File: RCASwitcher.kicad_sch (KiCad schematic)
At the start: 11 parts, among them J1 Connector_RCA_2x3_REB, J2 Connector_RCA_2x3_REB, J3 Connector_RCA_2x3_REB, J4 Connector_RCA_2x3_REB, J5 Connector_RCA_2x3_REB, J6 Connector_RCA_2x3_REB, SW1 SW_SPDT_3x2_REB, SW2 SW_SPDT_3x2_REB, SW3 SW_SPDT_3x2_REB, SW4 SW_SPDT_3x2_REB, SW5 SW_SPDT_3x2_REB

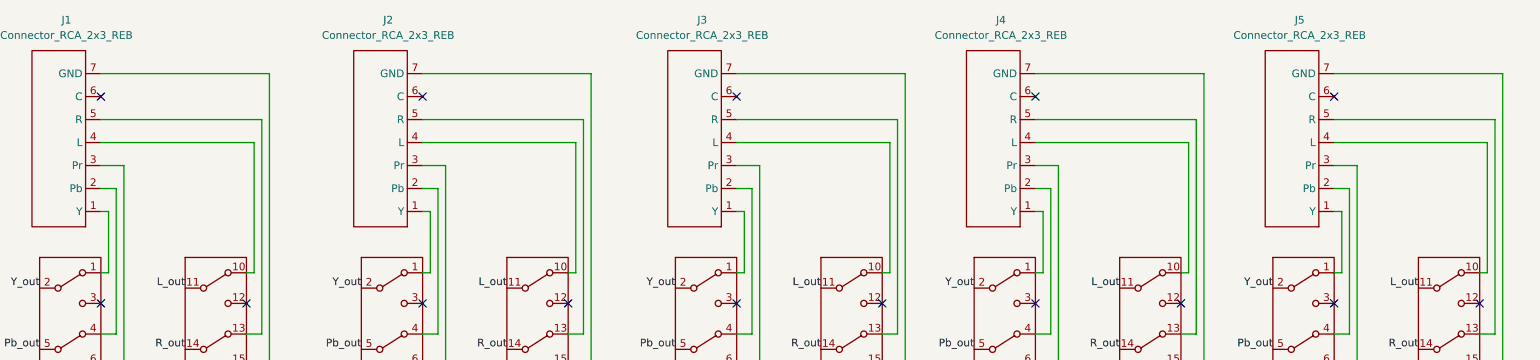
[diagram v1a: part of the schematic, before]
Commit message: Name remaining nets for checking
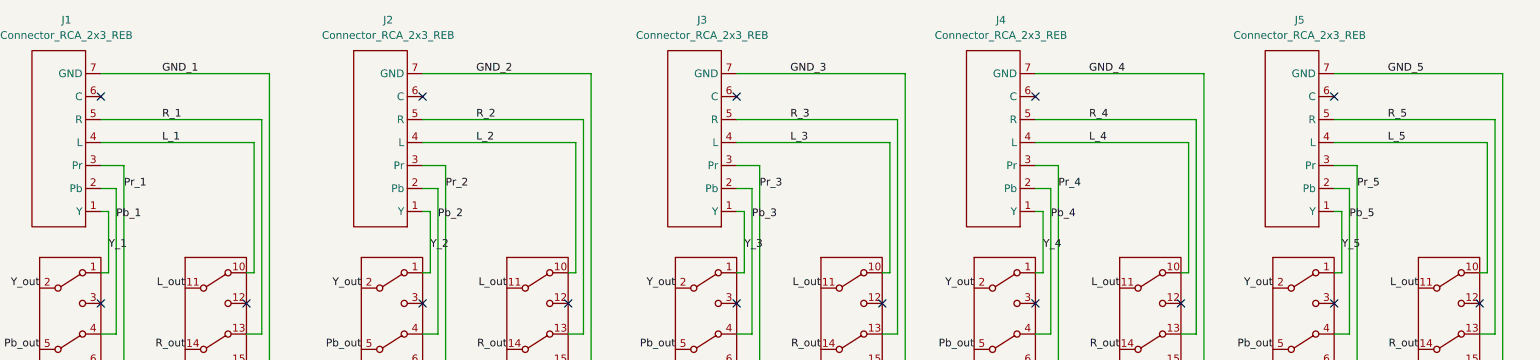
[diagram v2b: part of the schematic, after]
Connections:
- net Y_2: now reaches J2.1 (Y), SW2.1 (A)
- net Pb_2: now reaches J2.2 (Pb), SW2.4 (A)
- net Pr_2: now reaches J2.3 (Pr), SW2.7 (A)
- net L_2: now reaches J2.4 (L), SW2.10 (A)
- net R_2: now reaches J2.5 (R), SW2.13 (A)
- net GND_2: now reaches J2.7 (GND), J2.8 (GND), J2.9 (GND), SW2.16 (A)
- net Y_1: now reaches J1.1 (Y), SW1.1 (A)
- net L_1: now reaches J1.4 (L), SW1.10 (A)
- net R_1: now reaches J1.5 (R), SW1.13 (A)
- net GND_1: now reaches J1.7 (GND), J1.8 (GND), J1.9 (GND), SW1.16 (A)
- net Pb_1: now reaches J1.2 (Pb), SW1.4 (A)
- net Pr_1: now reaches J1.3 (Pr), SW1.7 (A)
- net Y_5: now reaches J5.1 (Y), SW5.1 (A)
- net L_5: now reaches J5.4 (L), SW5.10 (A)
- net R_5: now reaches J5.5 (R), SW5.13 (A)
- net GND_5: now reaches J5.7 (GND), J5.8 (GND), J5.9 (GND), SW5.16 (A)
- net Pb_5: now reaches J5.2 (Pb), SW5.4 (A)
- net Pr_5: now reaches J5.3 (Pr), SW5.7 (A)
- net Y_3: now reaches J3.1 (Y), SW3.1 (A)
- net Pb_3: now reaches J3.2 (Pb), SW3.4 (A)
- net Pr_3: now reaches J3.3 (Pr), SW3.7 (A)
- net L_3: now reaches J3.4 (L), SW3.10 (A)
- net R_3: now reaches J3.5 (R), SW3.13 (A)
- net GND_3: now reaches J3.7 (GND), J3.8 (GND), J3.9 (GND), SW3.16 (A)
- net Y_4: now reaches J4.1 (Y), SW4.1 (A)
- net Pb_4: now reaches J4.2 (Pb), SW4.4 (A)
- net Pr_4: now reaches J4.3 (Pr), SW4.7 (A)
- net L_4: now reaches J4.4 (L), SW4.10 (A)
- net R_4: now reaches J4.5 (R), SW4.13 (A)
- net GND_4: now reaches J4.7 (GND), J4.8 (GND), J4.9 (GND), SW4.16 (A)
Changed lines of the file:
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@@
     (effects (font (size 1.27 1.27)) (justify right bottom))
+  )
+  (label "R_2" (at 96.52 44.45 0)
+    (effects (font (size 1.27 1.27)) (justify left bottom))
   )
   (label "Pr_out" (at 241.3 134.62 180)
     (effects (font (size 1.27 1.27)) (justify right bottom))
+  )
+  (label "Pr_4" (at 193.04 55.88 0)
+    (effects (font (size 1.27 1.27)) (justify left bottom))
+  )
+  (label "L_4" (at 198.12 48.26 0)
+    (effects (font (size 1.27 1.27)) (justify left bottom))
   )
   (label "Pb_out" (at 77.47 82.55 180)
@@
     (effects (font (size 1.27 1.27)) (justify right bottom))
   )
+  (label "L_2" (at 96.52 48.26 0)
+    (effects (font (size 1.27 1.27)) (justify left bottom))
+  )
   (label "GND_out" (at 203.2 92.71 180)
     (effects (font (size 1.27 1.27)) (justify right bottom))
+  )
+  (label "L_1" (at 44.45 48.26 0)
+    (effects (font (size 1.27 1.27)) (justify left bottom))
+  )
+  (label "GND_2" (at 96.52 36.83 0)
+    (effects (font (size 1.27 1.27)) (justify left bottom))
+  )
+  (label "GND_1" (at 44.45 36.83 0)
+    (effects (font (size 1.27 1.27)) (justify left bottom))
   )
   (label "Pr_out" (at 24.13 92.71 180)
     (effects (font (size 1.27 1.27)) (justify right bottom))
   )
+  (label "Pb_5" (at 241.3 60.96 0)
+    (effects (font (size 1.27 1.27)) (justify left bottom))
+  )
   (label "R_out" (at 153.67 82.55 180)
     (effects (font (size 1.27 1.27)) (justify right bottom))
+  )
+  (label "Y_2" (at 88.9 66.04 0)
+    (effects (font (size 1.27 1.27)) (justify left bottom))
+  )
+  (label "Y_4" (at 190.5 66.04 0)
+    (effects (font (size 1.27 1.27)) (justify left bottom))
   )
   (label "GND_out" (at 252.73 92.71 180)
     (effects (font (size 1.27 1.27)) (justify right bottom))
   )
+  (label "R_4" (at 198.12 44.45 0)
+    (effects (font (size 1.27 1.27)) (justify left bottom))
+  )
+  (label "R_1" (at 44.45 44.45 0)
+    (effects (font (size 1.27 1.27)) (justify left bottom))
+  )
   (label "Y_out" (at 228.6 72.39 180)
     (effects (font (size 1.27 1.27)) (justify right bottom))
+  )
+  (label "R_3" (at 148.59 44.45 0)
+    (effects (font (size 1.27 1.27)) (justify left bottom))
+  )
+  (label "Pr_2" (at 91.44 55.88 0)
+    (effects (font (size 1.27 1.27)) (justify left bottom))
   )
   (label "Pb_out" (at 24.13 82.55 180)
@@
   (label "Pr_out" (at 228.6 92.71 180)
     (effects (font (size 1.27 1.27)) (justify right bottom))
+  )
+  (label "GND_4" (at 198.12 36.83 0)
+    (effects (font (size 1.27 1.27)) (justify left bottom))
   )
   (label "Y_out" (at 77.47 72.39 180)
@@
     (effects (font (size 1.27 1.27)) (justify right bottom))
   )
+  (label "Y_1" (at 35.56 66.04 0)
+    (effects (font (size 1.27 1.27)) (justify left bottom))
+  )
   (label "Pr_out" (at 129.54 92.71 180)
     (effects (font (size 1.27 1.27)) (justify right bottom))
+  )
+  (label "Y_5" (at 240.03 66.04 0)
+    (effects (font (size 1.27 1.27)) (justify left bottom))
   )
   (label "R_out" (at 203.2 82.55 180)
@@
     (effects (font (size 1.27 1.27)) (justify right bottom))
   )
+  (label "Pr_3" (at 143.51 55.88 0)
+    (effects (font (size 1.27 1.27)) (justify left bottom))
+  )
   (label "Y_out" (at 179.07 72.39 180)
     (effects (font (size 1.27 1.27)) (justify right bottom))
@@
   (label "Y_out" (at 129.54 72.39 180)
     (effects (font (size 1.27 1.27)) (justify right bottom))
+  )
+  (label "Y_3" (at 140.97 66.04 0)
+    (effects (font (size 1.27 1.27)) (justify left bottom))
+  )
+  (label "Pb_4" (at 191.77 60.96 0)
+    (effects (font (size 1.27 1.27)) (justify left bottom))
+  )
+  (label "R_5" (at 247.65 44.45 0)
+    (effects (font (size 1.27 1.27)) (justify left bottom))
+  )
+  (label "GND_3" (at 148.59 36.83 0)
+    (effects (font (size 1.27 1.27)) (justify left bottom))
+  )
+  (label "Pb_3" (at 142.24 60.96 0)
+    (effects (font (size 1.27 1.27)) (justify left bottom))
+  )
+  (label "Pr_1" (at 38.1 55.88 0)
+    (effects (font (size 1.27 1.27)) (justify left bottom))
   )
   (label "Y_out" (at 241.3 127 180)
@@
     (effects (font (size 1.27 1.27)) (justify right bottom))
   )
+  (label "L_3" (at 148.59 48.26 0)
+    (effects (font (size 1.27 1.27)) (justify left bottom))
+  )
   (label "L_out" (at 153.67 72.39 180)
     (effects (font (size 1.27 1.27)) (justify right bottom))
+  )
+  (label "Pr_5" (at 242.57 55.88 0)
+    (effects (font (size 1.27 1.27)) (justify left bottom))
   )
   (label "R_out" (at 241.3 142.24 180)
@@
   (label "GND_out" (at 48.26 92.71 180)
     (effects (font (size 1.27 1.27)) (justify right bottom))
+  )
+  (label "Pb_1" (at 36.83 60.96 0)
+    (effects (font (size 1.27 1.27)) (justify left bottom))
   )
   (label "L_out" (at 241.3 138.43 180)
@@
     (effects (font (size 1.27 1.27)) (justify right bottom))
   )
+  (label "Pb_2" (at 90.17 60.96 0)
+    (effects (font (size 1.27 1.27)) (justify left bottom))
+  )
+  (label "GND_5" (at 247.65 36.83 0)
+    (effects (font (size 1.27 1.27)) (justify left bottom))
+  )
   (label "GND_out" (at 153.67 92.71 180)
     (effects (font (size 1.27 1.27)) (justify right bottom))
@@
     (effects (font (size 1.27 1.27)) (justify right bottom))
   )
+  (label "L_5" (at 247.65 48.26 0)
+    (effects (font (size 1.27 1.27)) (justify left bottom))
+  )
   (symbol (lib_name "Connector_RCA_2x3_REB_4") (lib_id "User:Connector_RCA_2x3_REB") (at 92.71 62.23 180) (unit 1)

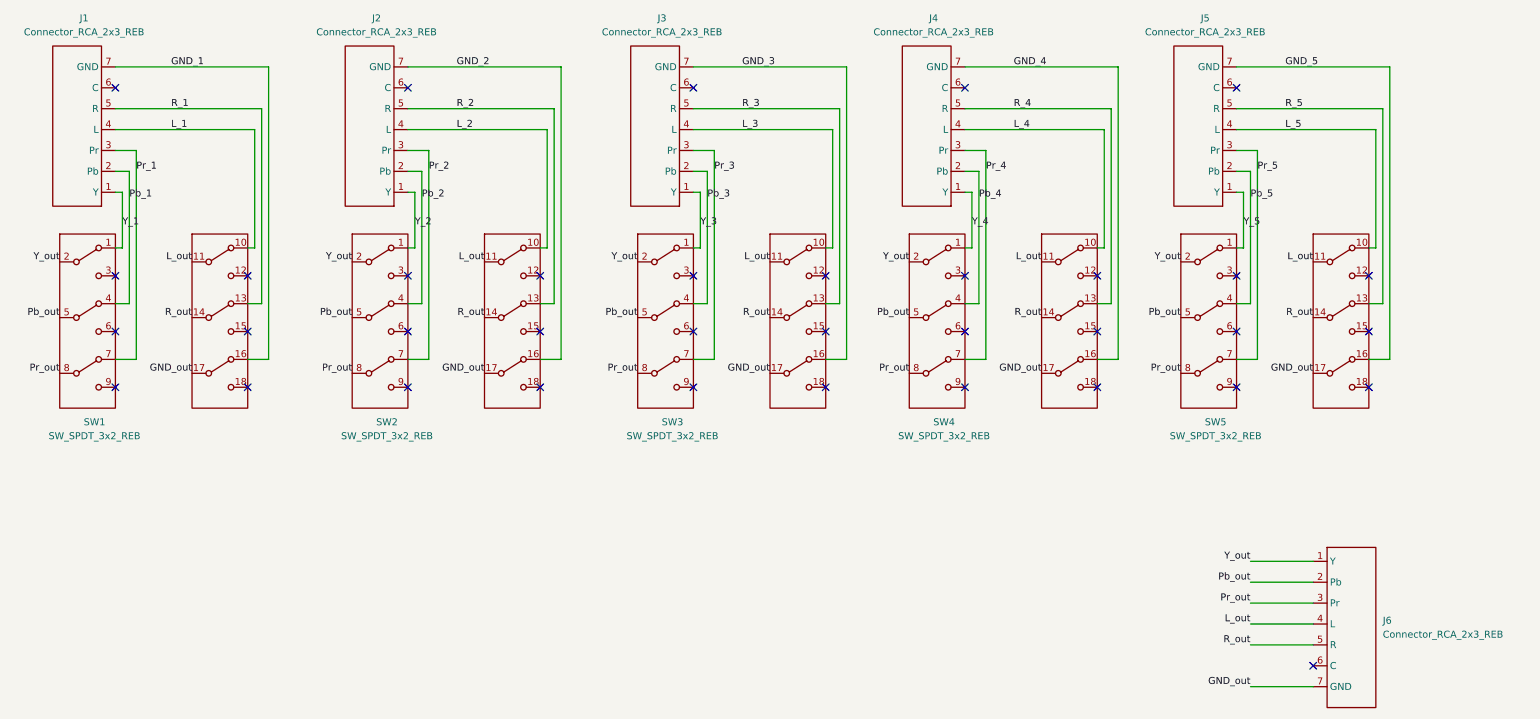
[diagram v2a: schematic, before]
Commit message: Reversing which side gets connected, tested with hand soldering
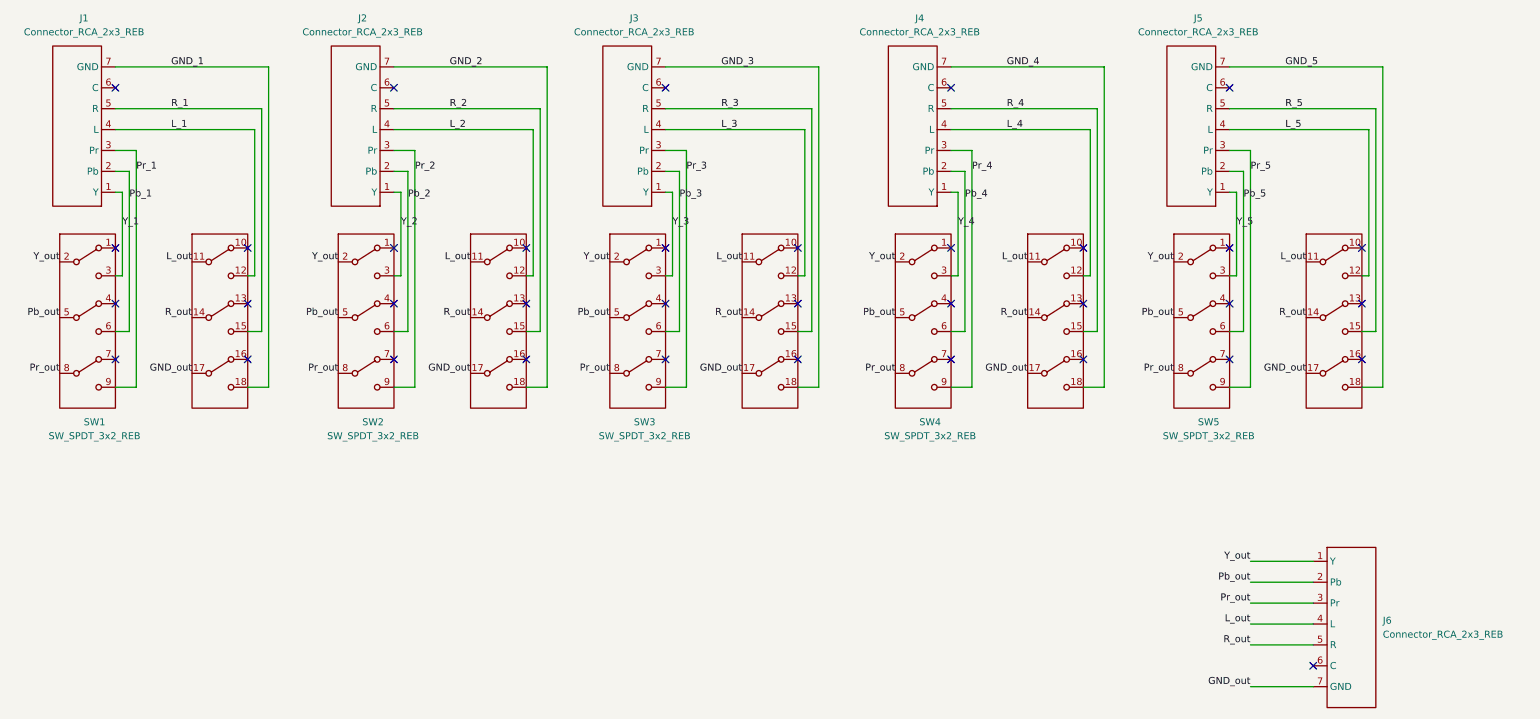
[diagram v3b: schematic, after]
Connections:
- net GND_1: now also SW1.18 (C); no longer SW1.16 (A)
- net GND_2: now also SW2.18 (C); no longer SW2.16 (A)
- net GND_3: now also SW3.18 (C); no longer SW3.16 (A)
- net GND_4: now also SW4.18 (C); no longer SW4.16 (A)
- net GND_5: now also SW5.18 (C); no longer SW5.16 (A)
- net L_1: now also SW1.12 (C); no longer SW1.10 (A)
- net L_2: now also SW2.12 (C); no longer SW2.10 (A)
- net L_3: now also SW3.12 (C); no longer SW3.10 (A)
- net L_4: now also SW4.12 (C); no longer SW4.10 (A)
- net L_5: now also SW5.12 (C); no longer SW5.10 (A)
- net Pb_1: now also SW1.6 (C); no longer SW1.4 (A)
- net Pb_2: now also SW2.6 (C); no longer SW2.4 (A)
- net Pb_3: now also SW3.6 (C); no longer SW3.4 (A)
- net Pb_4: now also SW4.6 (C); no longer SW4.4 (A)
- net Pb_5: now also SW5.6 (C); no longer SW5.4 (A)
- net Pr_1: now also SW1.9 (C); no longer SW1.7 (A)
- net Pr_2: now also SW2.9 (C); no longer SW2.7 (A)
- net Pr_3: now also SW3.9 (C); no longer SW3.7 (A)
- net Pr_4: now also SW4.9 (C); no longer SW4.7 (A)
- net Pr_5: now also SW5.9 (C); no longer SW5.7 (A)
- net R_1: now also SW1.15 (C); no longer SW1.13 (A)
- net R_2: now also SW2.15 (C); no longer SW2.13 (A)
- net R_3: now also SW3.15 (C); no longer SW3.13 (A)
- net R_4: now also SW4.15 (C); no longer SW4.13 (A)
- net R_5: now also SW5.15 (C); no longer SW5.13 (A)
- net Y_1: now also SW1.3 (C); no longer SW1.1 (A)
- net Y_2: now also SW2.3 (C); no longer SW2.1 (A)
- net Y_3: now also SW3.3 (C); no longer SW3.1 (A)
- net Y_4: now also SW4.3 (C); no longer SW4.1 (A)
- net Y_5: now also SW5.3 (C); no longer SW5.1 (A)
